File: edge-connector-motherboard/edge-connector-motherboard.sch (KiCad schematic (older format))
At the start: 15 parts, among them J1 Screw_Terminal_1x01, J10 Screw_Terminal_1x01, J11 Screw_Terminal_1x01, J12 Screw_Terminal_1x01, J13 Screw_Terminal_1x01, J14 Screw_Terminal_1x01, J15 Screw_Terminal_1x01, J2 Screw_Terminal_1x01, J3 Screw_Terminal_1x01, J4 Screw_Terminal_1x01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

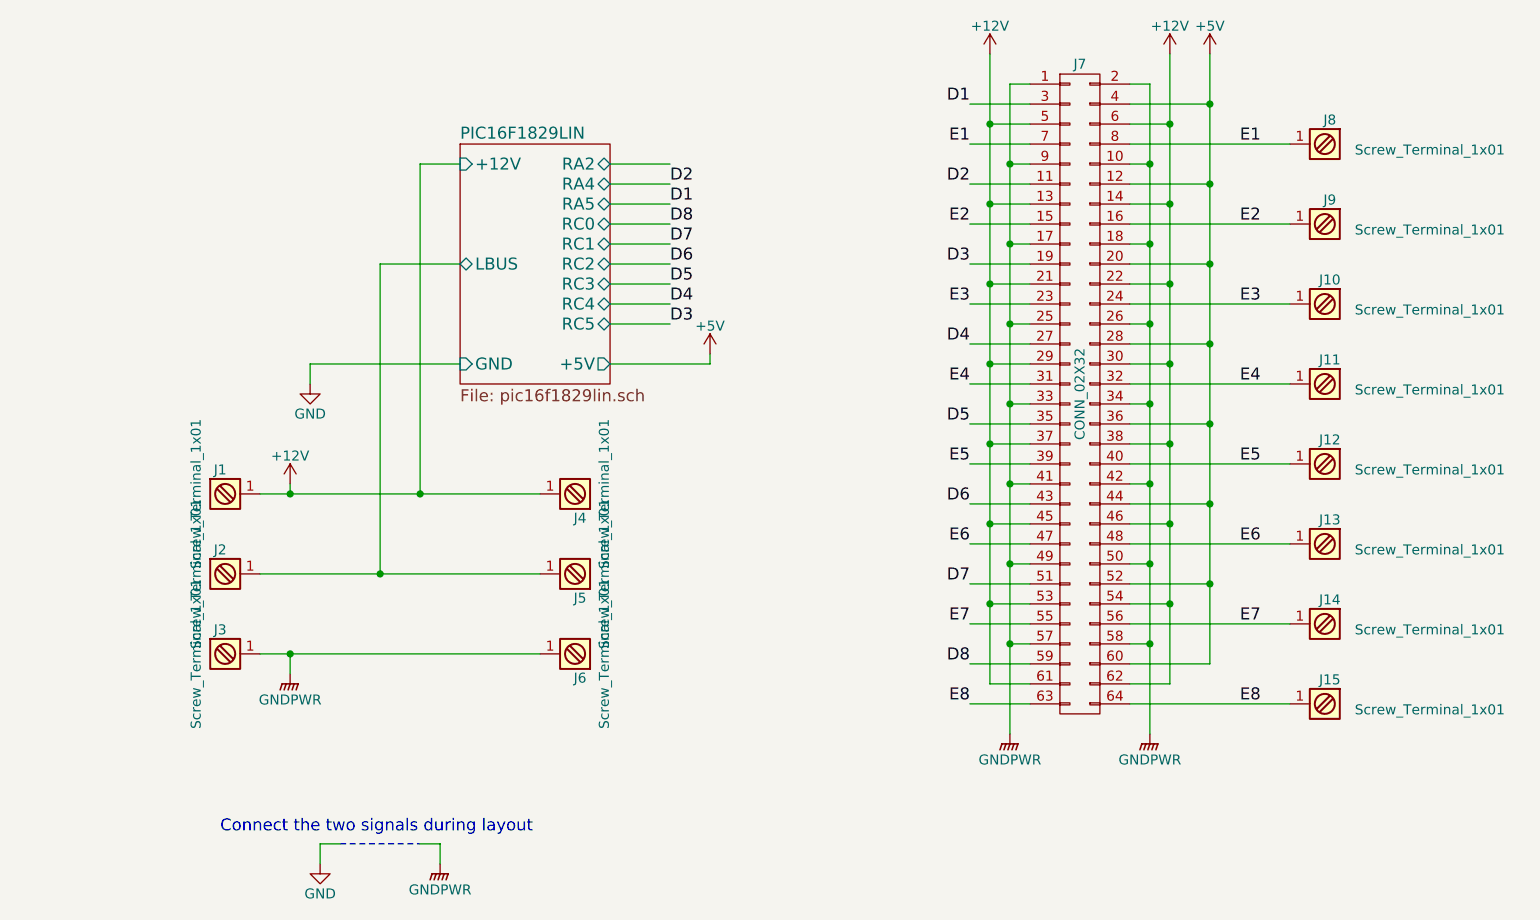
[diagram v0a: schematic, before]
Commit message: edge-connector-motherboard: adding 3d models and digikey references
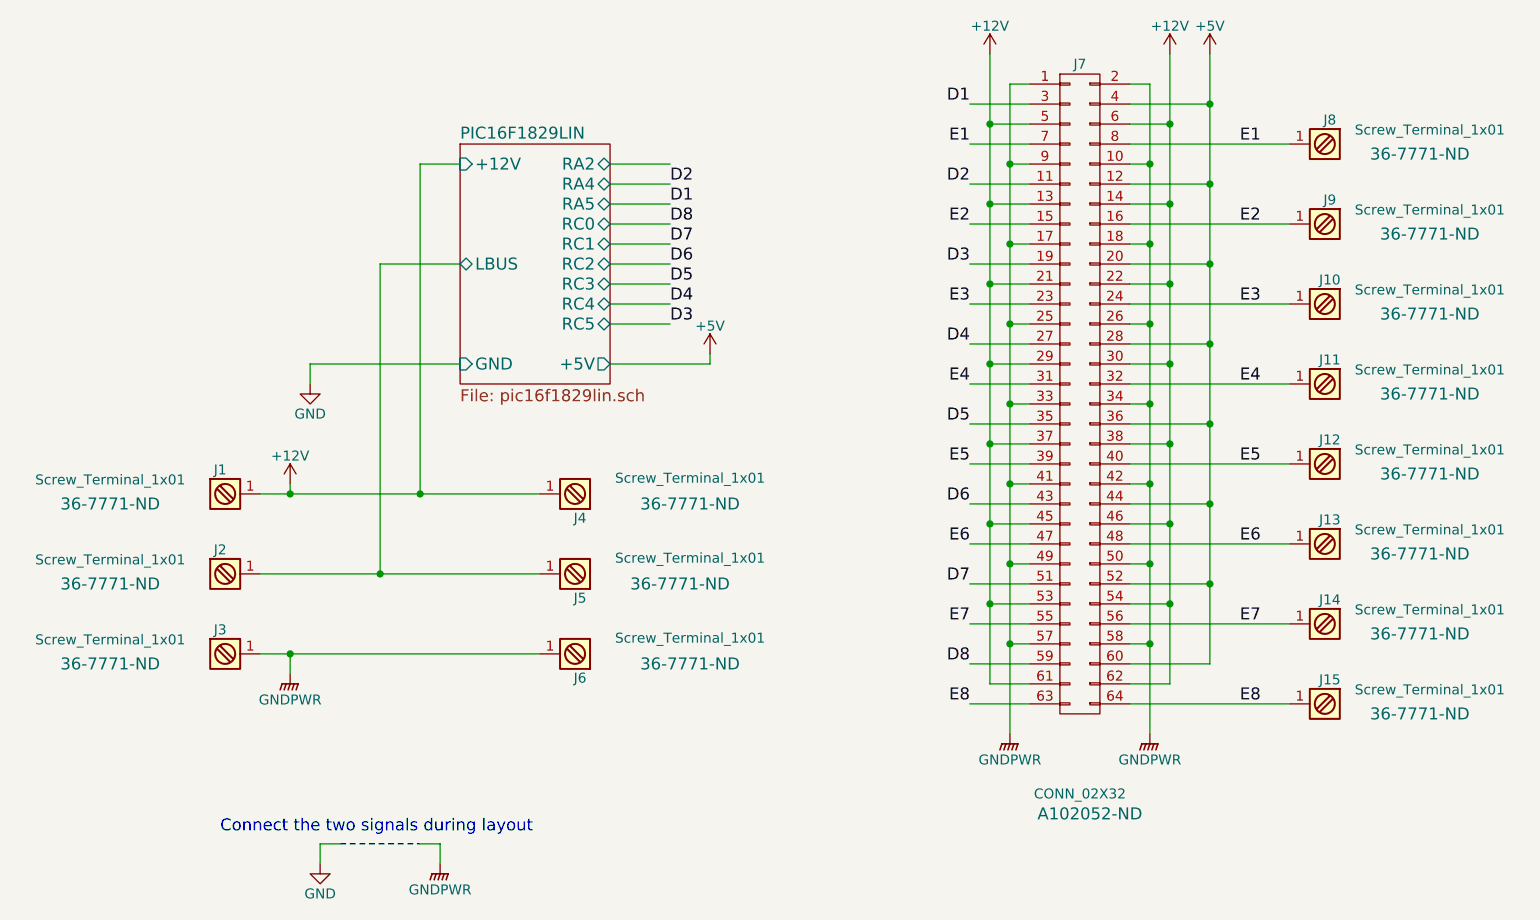
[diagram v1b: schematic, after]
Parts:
- J1, J10, J11, J12, J13, J14, J15, J2, J3, J4, J5, J6, J9: DIGIKEY (none) -> 36-7771-ND
- J8: DIGIKEY 36-7770-ND -> 36-7771-ND
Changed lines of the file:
@@
 P 3000 4250
 F 0 "J1" H 3000 4400 50  0000 C TNN
-F 1 "Screw_Terminal_1x01" V 2850 4250 50  0000 C TNN
+F 1 "Screw_Terminal_1x01" H 2450 4350 50  0000 C TNN
 F 2 "edge-connector-motherboard:TERM_SCREW_M3" H 3000 4125 50  0001 C CNN
 F 3 "" H 3000 4150 50  0001 C CNN
+F 4 "36-7771-ND" H 2450 4200 60  0000 C CNN "DIGIKEY"
 	1    3000 4250
 	1    0    0    -1
@@
 P 3000 4650
 F 0 "J2" H 3000 4800 50  0000 C TNN
-F 1 "Screw_Terminal_1x01" V 2850 4650 50  0000 C TNN
+F 1 "Screw_Terminal_1x01" H 2450 4750 50  0000 C TNN
 F 2 "edge-connector-motherboard:TERM_SCREW_M3" H 3000 4525 50  0001 C CNN
 F 3 "" H 3000 4550 50  0001 C CNN
+F 4 "36-7771-ND" H 2450 4600 60  0000 C CNN "DIGIKEY"
 	1    3000 4650
 	1    0    0    -1
@@
 P 3000 5050
 F 0 "J3" H 3000 5200 50  0000 C TNN
-F 1 "Screw_Terminal_1x01" V 2850 5050 50  0000 C TNN
+F 1 "Screw_Terminal_1x01" H 2450 5150 50  0000 C TNN
 F 2 "edge-connector-motherboard:TERM_SCREW_M3" H 3000 4925 50  0001 C CNN
 F 3 "" H 3000 4950 50  0001 C CNN
+F 4 "36-7771-ND" H 2450 5000 60  0000 C CNN "DIGIKEY"
 	1    3000 5050
 	1    0    0    -1
@@
 P 4800 4250
 F 0 "J4" H 4800 4400 50  0000 C TNN
-F 1 "Screw_Terminal_1x01" V 4650 4250 50  0000 C TNN
+F 1 "Screw_Terminal_1x01" H 4250 4200 50  0000 C TNN
 F 2 "edge-connector-motherboard:TERM_SCREW_M3" H 4800 4125 50  0001 C CNN
 F 3 "" H 4800 4150 50  0001 C CNN
+F 4 "36-7771-ND" H 4250 4300 60  0000 C CNN "DIGIKEY"
 	1    4800 4250
 	-1   0    0    1
@@
 P 4800 4650
 F 0 "J5" H 4800 4800 50  0000 C TNN
-F 1 "Screw_Terminal_1x01" V 4650 4650 50  0000 C TNN
+F 1 "Screw_Terminal_1x01" H 4250 4600 50  0000 C TNN
 F 2 "edge-connector-motherboard:TERM_SCREW_M3" H 4800 4525 50  0001 C CNN
 F 3 "" H 4800 4550 50  0001 C CNN
+F 4 "36-7771-ND" H 4300 4700 60  0000 C CNN "DIGIKEY"
 	1    4800 4650
 	-1   0    0    1
@@
 P 4800 5050
 F 0 "J6" H 4800 5200 50  0000 C TNN
-F 1 "Screw_Terminal_1x01" V 4650 5050 50  0000 C TNN
+F 1 "Screw_Terminal_1x01" H 4250 5000 50  0000 C TNN
 F 2 "edge-connector-motherboard:TERM_SCREW_M3" H 4800 4925 50  0001 C CNN
 F 3 "" H 4800 4950 50  0001 C CNN
+F 4 "36-7771-ND" H 4250 5100 60  0000 C CNN "DIGIKEY"
 	1    4800 5050
 	-1   0    0    1
@@
 P 7300 3750
 F 0 "J7" H 7300 5400 50  0000 C CNN
-F 1 "CONN_02X32" V 7300 3750 50  0000 C CNN
+F 1 "CONN_02X32" H 7300 1750 50  0000 C CNN
 F 2 "Pin_Headers:Pin_Header_Angled_2x32_Pitch2.54mm" H 7300 3350 50  0001 C CNN
 F 3 "http://www.te.com/commerce/DocumentDelivery/DDEController?Action=showdoc&DocId=Customer+Drawing%7F1761468%7FC2%7Fpdf%7FEnglish%7FENG_CD_1761468_C2.pdf%7F1761468-1" H 7300 3350 50  0001 C CNN
-F 4 "A102052-ND" H 7300 3750 60  0001 C CNN "DIGIKEY"
+F 4 "A102052-ND" H 7350 1650 60  0000 C CNN "DIGIKEY"
 	1    7300 3750
 	1    0    0    -1
@@
 P 8550 3700
 F 0 "J11" H 8550 3850 50  0000 C TNN
-F 1 "Screw_Terminal_1x01" H 8050 3700 50  0000 C TNN
+F 1 "Screw_Terminal_1x01" H 8050 3800 50  0000 C TNN
 F 2 "edge-connector-motherboard:TERM_SCREW_M3" H 8550 3575 50  0001 C CNN
 F 3 "" H 8550 3600 50  0001 C CNN
+F 4 "36-7771-ND" H 8050 3650 60  0000 C CNN "DIGIKEY"
 	1    8550 3700
 	-1   0    0    -1
@@
 P 8550 3300
 F 0 "J10" H 8550 3450 50  0000 C TNN
-F 1 "Screw_Terminal_1x01" H 8050 3300 50  0000 C TNN
+F 1 "Screw_Terminal_1x01" H 8050 3400 50  0000 C TNN
 F 2 "edge-connector-motherboard:TERM_SCREW_M3" H 8550 3175 50  0001 C CNN
 F 3 "" H 8550 3200 50  0001 C CNN
+F 4 "36-7771-ND" H 8050 3250 60  0000 C CNN "DIGIKEY"
 	1    8550 3300
 	-1   0    0    -1
@@
 P 8550 2900
 F 0 "J9" H 8550 3050 50  0000 C TNN
-F 1 "Screw_Terminal_1x01" H 8050 2900 50  0000 C TNN
+F 1 "Screw_Terminal_1x01" H 8050 3000 50  0000 C TNN
 F 2 "edge-connector-motherboard:TERM_SCREW_M3" H 8550 2775 50  0001 C CNN
 F 3 "" H 8550 2800 50  0001 C CNN
+F 4 "36-7771-ND" H 8050 2850 60  0000 C CNN "DIGIKEY"
 	1    8550 2900
 	-1   0    0    -1
@@
 P 8550 2500
 F 0 "J8" H 8550 2650 50  0000 C TNN
-F 1 "Screw_Terminal_1x01" H 8050 2500 50  0000 C TNN
+F 1 "Screw_Terminal_1x01" H 8050 2600 50  0000 C TNN
 F 2 "edge-connector-motherboard:TERM_SCREW_M3" H 8550 2375 50  0001 C CNN
 F 3 "http://www.keyelco.com/product-pdf.cfm?p=1090" H 8550 2400 50  0001 C CNN
-F 4 "36-7770-ND" H 8550 2500 60  0001 C CNN "DIGIKEY"
+F 4 "36-7771-ND" H 8100 2450 60  0000 C CNN "DIGIKEY"
 	1    8550 2500
 	-1   0    0    -1
@@
 P 8550 5300
 F 0 "J15" H 8550 5450 50  0000 C TNN
-F 1 "Screw_Terminal_1x01" H 8050 5300 50  0000 C TNN
+F 1 "Screw_Terminal_1x01" H 8050 5400 50  0000 C TNN
 F 2 "edge-connector-motherboard:TERM_SCREW_M3" H 8550 5175 50  0001 C CNN
 F 3 "" H 8550 5200 50  0001 C CNN
+F 4 "36-7771-ND" H 8100 5250 60  0000 C CNN "DIGIKEY"
 	1    8550 5300
 	-1   0    0    -1
@@
 P 8550 4900
 F 0 "J14" H 8550 5050 50  0000 C TNN
-F 1 "Screw_Terminal_1x01" H 8050 4900 50  0000 C TNN
+F 1 "Screw_Terminal_1x01" H 8050 5000 50  0000 C TNN
 F 2 "edge-connector-motherboard:TERM_SCREW_M3" H 8550 4775 50  0001 C CNN
 F 3 "" H 8550 4800 50  0001 C CNN
+F 4 "36-7771-ND" H 8100 4850 60  0000 C CNN "DIGIKEY"
 	1    8550 4900
 	-1   0    0    -1
@@
 P 8550 4500
 F 0 "J13" H 8550 4650 50  0000 C TNN
-F 1 "Screw_Terminal_1x01" H 8050 4500 50  0000 C TNN
+F 1 "Screw_Terminal_1x01" H 8050 4600 50  0000 C TNN
 F 2 "edge-connector-motherboard:TERM_SCREW_M3" H 8550 4375 50  0001 C CNN
 F 3 "" H 8550 4400 50  0001 C CNN
+F 4 "36-7771-ND" H 8100 4450 60  0000 C CNN "DIGIKEY"
 	1    8550 4500
 	-1   0    0    -1
@@
 P 8550 4100
 F 0 "J12" H 8550 4250 50  0000 C TNN
-F 1 "Screw_Terminal_1x01" H 8050 4100 50  0000 C TNN
+F 1 "Screw_Terminal_1x01" H 8050 4200 50  0000 C TNN
 F 2 "edge-connector-motherboard:TERM_SCREW_M3" H 8550 3975 50  0001 C CNN
 F 3 "" H 8550 4000 50  0001 C CNN
+F 4 "36-7771-ND" H 8050 4050 60  0000 C CNN "DIGIKEY"
 	1    8550 4100
 	-1   0    0    -1
